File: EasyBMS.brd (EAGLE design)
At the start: 49 x 100 mm, 151 parts, among them IC1 LM2596S-5.0_NOPB, IC2 LTC6811IG-1#PBF, IC3 ESP32-S3-WROOM-1-N4R2, IC4 DRV103H, Q10 BSS84LT1G, Q11 BSS84LT1G, Q12 BSS84LT1G, Q13 BSS84LT1G, Q2 BSS84LT1G, Q3 BSS84LT1G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

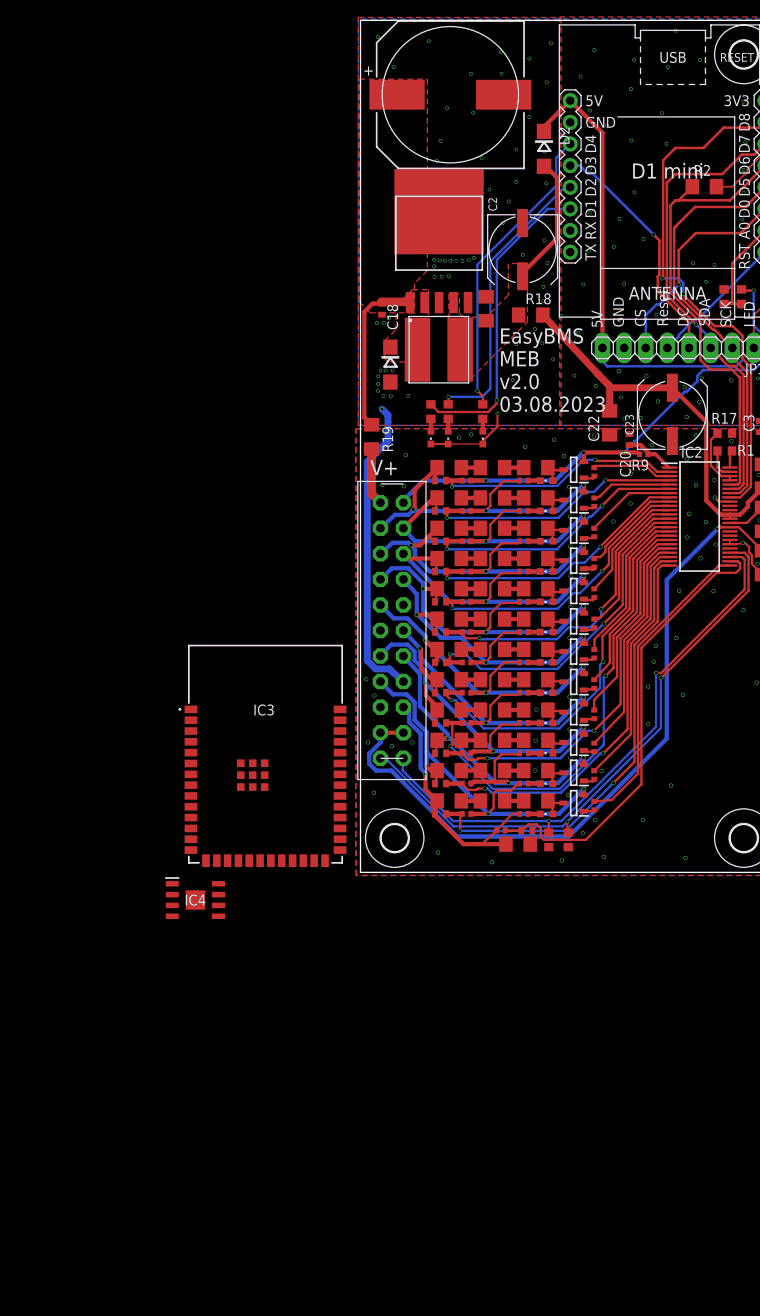
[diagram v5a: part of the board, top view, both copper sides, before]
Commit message: new parts for DC DC added
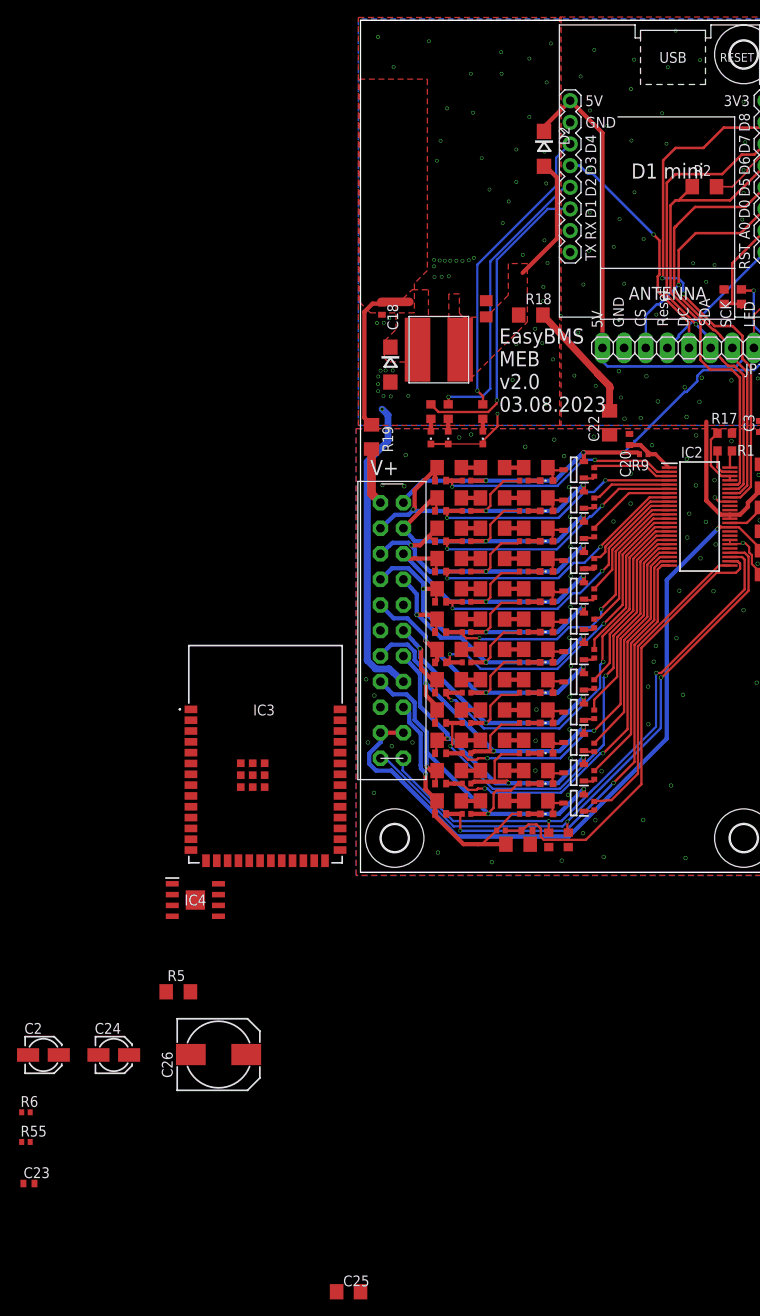
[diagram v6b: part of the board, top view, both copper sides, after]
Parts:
- removed IC1: LM2596S-5.0_NOPB, SamacSys_Parts:KTT0005B
- added C25: 1uF, rcl:C1206
- added C26: (no value), rcl:140CLH-0810
- added R5: R082, rcl:R1206
- added R55: 3k3, rcl:R0402
- added R6: 10k, rcl:R0402
- C2: value C249880 -> (none); device rcl:UD-8X10_NICHICON -> rcl:153CLV-0405
- C21: value 1uF -> 100nF; device rcl:C1206 -> rcl:C0805
- C23: value C249880 -> 10nF; device rcl:UD-8X10_NICHICON -> rcl:C0402
- C24: value C249935 -> (none); device SamacSys_Parts:WCAP-ASLI_16X17(DXL) -> rcl:153CLV-0405
- moved C24 119.4 mm to (-29.0, -21.4), turned to 0 degrees
- moved C23 117.7 mm to (-38.9, -36.5), turned to 0 degrees
- moved C2 110.0 mm to (-37.2, -21.4), turned to 0 degrees
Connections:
- new net FB: C23.2, IC4.8, R55.2, R6.1
- new net N$3: C25.1, IC4.3
- new net N$5: IC4.2, L1.P$2, R5.1
- net +5V: now also C2.+; no longer C23.+
- net +5V/1: now also C23.1, C24.+, IC4.1, R5.2, R6.2; no longer C2.+, IC1.4, L1.P$2
- net GND: now also C24.-, C26.-, IC4.6, IC4.7, R55.1; no longer C2.-, C24.2, IC1.3, IC1.5, IC1.6
- net GND2: now also C2.-; no longer C23.-
- net N$17: now also IC4.5; no longer IC1.2
- net N$75: now also C25.2, C26.+, IC4.4; no longer C24.1, IC1.1
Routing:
- net +5V: track 48.1 -> 35.2 mm

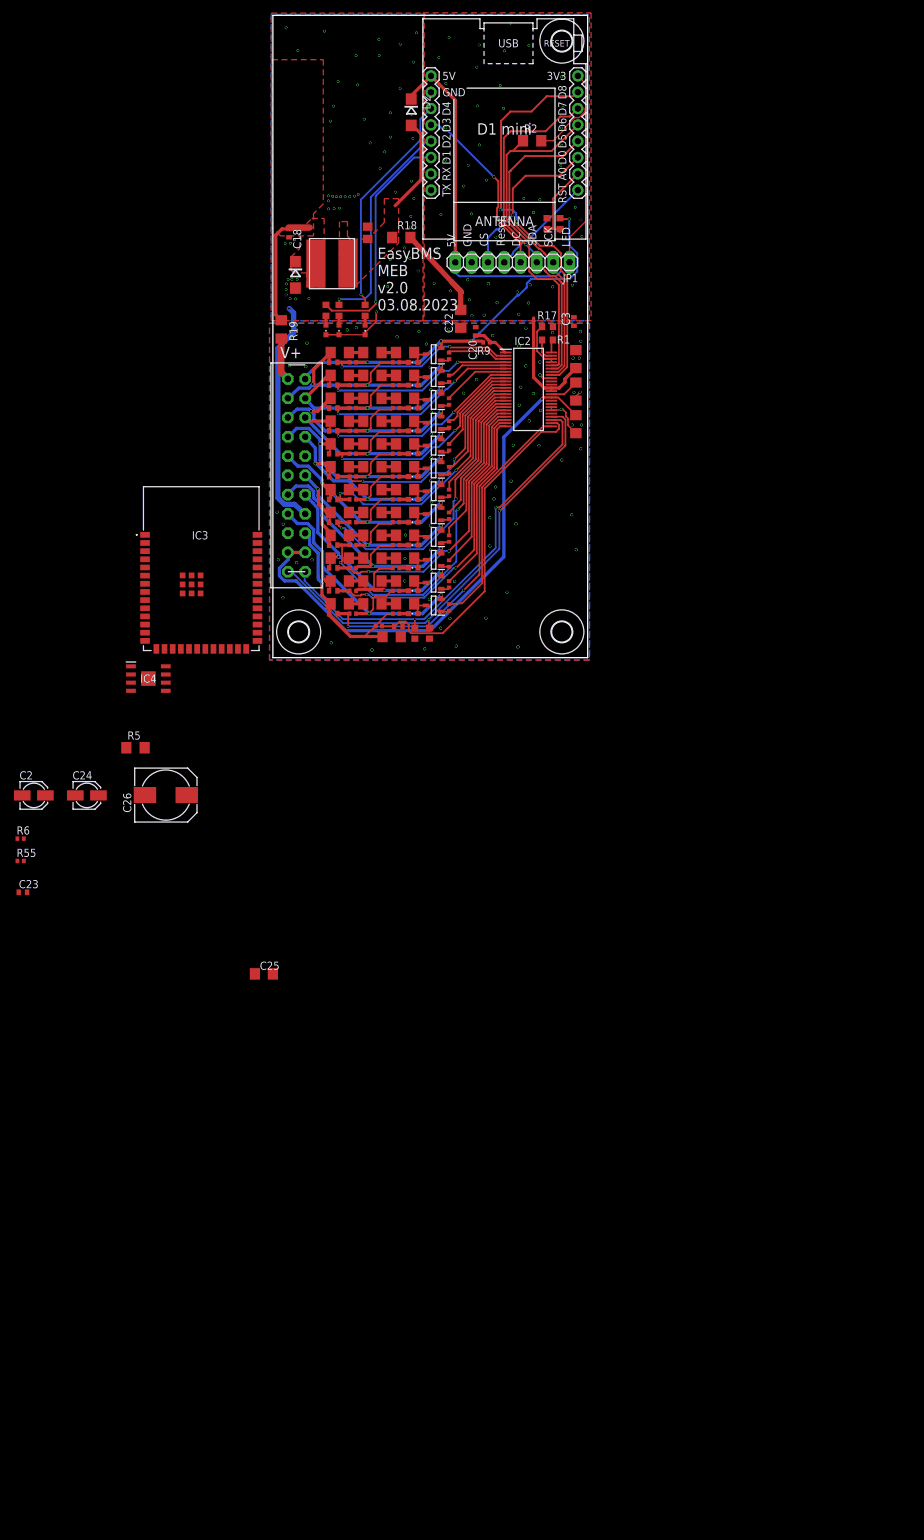
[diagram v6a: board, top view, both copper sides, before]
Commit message: XL7046 properly added
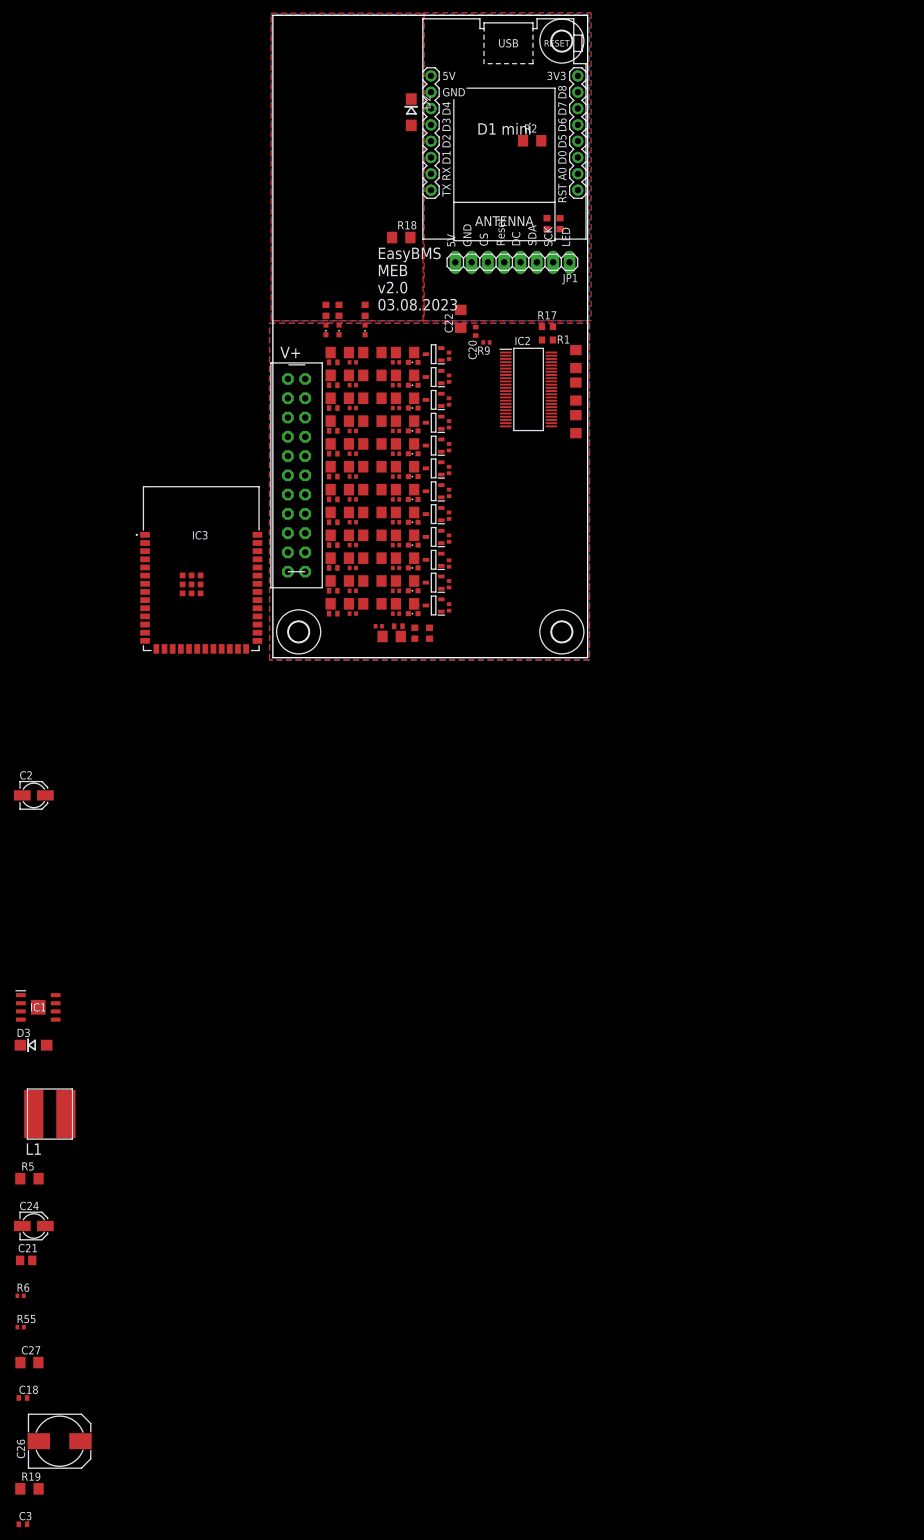
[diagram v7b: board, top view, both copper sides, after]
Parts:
- removed C23: 10nF, rcl:C0402
- removed C25: 1uF, rcl:C1206
- removed D1: C16015, diode:DO214AC
- removed IC4: DRV103H, SamacSys_Parts:SOIC127P600X170-9N
- added C27: 1uF, rcl:C1206
- added D3: C16015, diode:DO214AC
- added IC1: XL7046, SamacSys_Parts:SOIC127P600X170-9N
- moved C3 205.9 mm to (-38.9, -134.9), turned to 0 degrees
- moved C18 186.0 mm to (-38.9, -115.2), turned to 0 degrees
- moved R19 184.7 mm to (-37.9, -129.4), turned to 0 degrees
- moved C21 168.6 mm to (-38.4, -93.8), turned to 0 degrees
- moved L1 139.5 mm to (-34.7, -71.0)
- moved C26 101.9 mm to (-33.2, -122.0)
- moved R55 72.6 mm to (-39.3, -104.2)
- moved R6 71.2 mm to (-39.3, -99.3)
- moved R5 69.1 mm to (-37.9, -81.1)
- moved C24 67.5 mm to (-37.2, -88.5)
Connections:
- removed net FB: C23.2, IC4.8, R55.2, R6.1
- removed net N$17: D1.C, IC4.5, L1.P$1
- removed net N$3: C25.1, IC4.3
- removed net N$5: IC4.2, L1.P$2, R5.1
- removed net N$75: C18.1, C25.2, C26.+, IC4.4, R19.1
- new net N$15: IC1.2, L1.P$2, R5.1
- new net N$25: IC1.8, R55.2, R6.1
- new net N$6: C27.2, IC1.3
- new net N$7: D3.C, IC1.5, L1.P$1
- new net N$73: C18.1, C26.+, C27.1, IC1.4, R19.1
- net +5V/1: now also IC1.1; no longer C23.1, IC4.1
- net GND: now also D3.A, IC1.7; no longer D1.A, IC4.6, IC4.7
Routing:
- net VREF2: track 83.7 -> 0.00 mm, vias 1 -> 0
- net VTEMP2: track 69.1 -> 0.00 mm, vias 2 -> 0
- net VTEMP1: track 65.7 -> 0.00 mm, vias 2 -> 0
- net C12+: track 65.1 -> 0.00 mm, vias 4 -> 0
- net CSLTC: track 61.8 -> 0.00 mm, vias 2 -> 0
- net C4: track 55.1 -> 0.00 mm, vias 2 -> 0
- net MOSI: track 54.8 -> 0.00 mm, vias 1 -> 0
- net 5VINESP: track 54.1 -> 0.00 mm
- net MISO: track 54.0 -> 0.00 mm
- net C0: track 53.6 -> 0.00 mm
- net C1: track 53.0 -> 0.00 mm, vias 2 -> 0
- net SCK: track 49.0 -> 0.00 mm
- net C2: track 48.8 -> 0.00 mm, vias 2 -> 0
- net C1+: track 47.8 -> 0.00 mm, vias 3 -> 0
- net C3+: track 47.1 -> 0.00 mm, vias 3 -> 0
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- removed copper zone on layer 1, net +5V/1
- removed copper zone on layer 1, net N$17
- removed copper zone on layer 1, net N$75

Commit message: balancer path reworked2
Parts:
- removed U$2: WEMOS-D1-MINI, diy-modules:WEMOS-D1-MINI
- added C25, C29: 10nF, rcl:C0402
- added D4, D6: (no value), semicon-smd-ipc:MELF-MLL34
- added Q14, Q16: C8547, SamacSys_Parts:PG-SOT-23
- added R103, R104, R82, R96: 10R0, rcl:R1206
- added R105, R97: 3.3k, rcl:R0402
- added R106, R98: 100R, rcl:R0402
- moved C26 214.3 mm to (8.26, 88.3)
- moved IC1 157.6 mm to (12.0, 95.5)
- moved L1 155.6 mm to (8.08, 78.6), turned to 90 degrees
- moved IC3 108.2 mm to (71.6, 83.4)
- moved R15 54.1 mm to (96.6, 52.0)
- moved JP1 54.1 mm to (89.2, 46.0)
- moved R16 54.1 mm to (94.5, 52.0)
- moved R2 33.3 mm to (64.7, 57.7)
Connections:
- new net C: C25.1, C29.1, D4.1, D6.1, R106.1, R98.1
- new net LOWER: C25.2, C29.2, D4.2, D6.2, R103.1, R82.1
- new net N$18: R82.2, R96.1
- new net N$75: Q14.3, R96.2
- new net N$76: Q14.1, R97.2
- new net N$80: R103.2, R104.1
- new net N$81: Q16.3, R104.2
- new net N$82: Q16.1, R105.2
- new net S: R105.1, R97.1
- new net UPPER: Q14.2, Q16.2, R106.2, R98.2
- net +3V3: no longer U$2.JP1.8
- net 5VINESP: no longer U$2.JP2.8
- net A0IN: no longer U$2.JP1.2
- net CSDSPL: no longer U$2.JP1.3
- net CSLTC: no longer U$2.JP1.7
- net D3: no longer U$2.JP2.5
- net GND: now also IC1.6, IC1.9; no longer U$2.JP2.7
- net MISO: no longer U$2.JP1.5
- net MOSI: no longer U$2.JP1.6
- net N$124: no longer U$2.JP2.4
- net N$30: no longer U$2.JP2.6
- net N$70: no longer U$2.JP2.3
- net RESET: no longer U$2.JP1.1
- net SCK: no longer U$2.JP1.4
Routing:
- net UPPER: track 0.00 -> 13.1 mm, vias 0 -> 2
- net C: track 0.00 -> 6.82 mm
- net LOWER: track 0.00 -> 4.13 mm
- net N$81: track 0.00 -> 2.33 mm
- net N$75: track 0.00 -> 2.33 mm
- net N$82: track 0.00 -> 2.17 mm
- net N$76: track 0.00 -> 2.17 mm
- added copper zone on layer 1, net N$18
- added copper zone on layer 16, net N$18
- added copper zone on layer 1, net N$80
- added copper zone on layer 16, net N$80
